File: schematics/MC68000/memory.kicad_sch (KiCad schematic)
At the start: 17 parts, among them J1 Conn_02x37_Row_Letter_Last, U13 ROM_LOW, U14 ROM_HIGH, U15 RAM_LOW, U16 RAM_HIGH, U17 GAL20V8, U27 74LS574

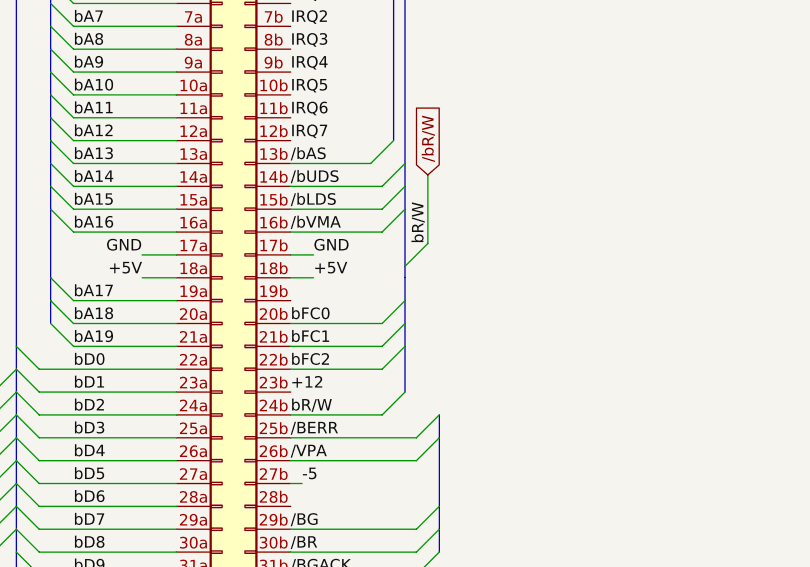
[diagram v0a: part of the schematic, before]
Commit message: Atmega8 code completed
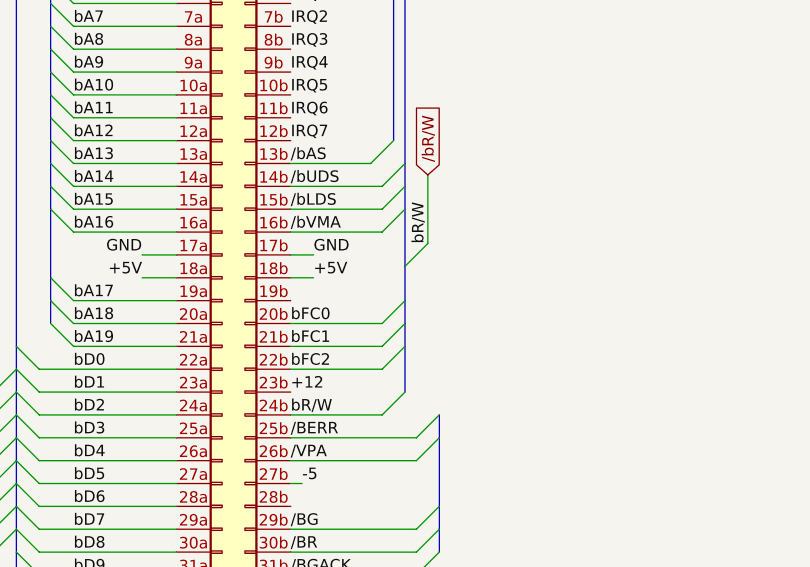
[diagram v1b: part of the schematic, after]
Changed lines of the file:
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@@
     (stroke (width 0) (type default))
   )
-  (bus (pts (xy 279.4 90.17) (xy 279.4 91.44))
+  (bus (pts (xy 279.4 90.17) (xy 279.4 93.98))
     (stroke (width 0) (type default))
   )
@@
     (stroke (width 0) (type default))
   )
-  (bus (pts (xy 279.4 91.44) (xy 279.4 93.98))
-    (stroke (width 0) (type default))
-  )

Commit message: Added ch376s
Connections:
- net /CH376S: now reaches J1.32b (Pin_32b)
- net /CH376S: now also U17.20 (I020)
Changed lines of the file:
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@@
 		)
 	)
+	(wire
+		(pts
+			(xy 266.7 127) (xy 271.78 127)
+		)
+		(stroke
+			(width 0)
+			(type default)
+		)
+	)
 	(bus
 		(pts
@@
 	(wire
 		(pts
+			(xy 106.68 123.19) (xy 99.06 123.19)
+		)
+		(stroke
+			(width 0)
+			(type default)
+		)
+	)
+	(wire
+		(pts
 			(xy 238.76 137.16) (xy 254 137.16)
 		)
@@
 	)
 	(global_label "{slash}IO_CS"
-		(shape input)
+		(shape output)
 		(at 106.68 120.65 0)
 		(fields_autoplaced yes)
@@
 		)
 	)
-	(global_label "{slash}ROM_CE"
+	(global_label "{slash}CH376S"
 		(shape input)
+		(at 271.78 127 0)
+		(fields_autoplaced yes)
+		(effects
+			(font
+				(size 1.27 1.27)
+			)
+			(justify left)
+		)
+		(property "Intersheetrefs" "${INTERSHEET_REFS}"
+			(at 283.5342 127 0)
+			(effects
+				(font
+					(size 1.27 1.27)
+				)
+				(justify left)
+				(hide yes)
+			)
+		)
+	)
+	(global_label "{slash}CH376S"
+		(shape output)
+		(at 106.68 123.19 0)
+		(fields_autoplaced yes)
+		(effects
+			(font
+				(size 1.27 1.27)
+			)
+			(justify left)
+		)
+		(property "Intersheetrefs" "${INTERSHEET_REFS}"
+			(at 118.4342 123.19 0)
+			(effects
+				(font
+					(size 1.27 1.27)
+				)
+				(justify left)
+				(hide yes)
+			)
+		)
+	)
+	(global_label "{slash}ROM_CE"
+		(shape output)
 		(at 106.68 118.11 0)
 		(fields_autoplaced yes)
@@
 	)
 	(global_label "{slash}DTACK"
-		(shape input)
+		(shape output)
 		(at 106.68 135.89 0)
 		(fields_autoplaced yes)
@@
 	)
 	(global_label "LEDS"
-		(shape input)
+		(shape output)
 		(at 106.68 133.35 0)
 		(fields_autoplaced yes)
@@
 	)
 	(global_label "{slash}RAM1CS_H"
-		(shape input)
+		(shape output)
 		(at 106.68 125.73 0)
 		(fields_autoplaced yes)
@@
 	)
 	(global_label "{slash}RAM1CS_L"
-		(shape input)
+		(shape output)
 		(at 106.68 128.27 0)
 		(fields_autoplaced yes)
